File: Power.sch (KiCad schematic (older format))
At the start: 38 parts, among them J17 Power Input, Q4 YJS9435A, U6 A4403, U7 MCP16301

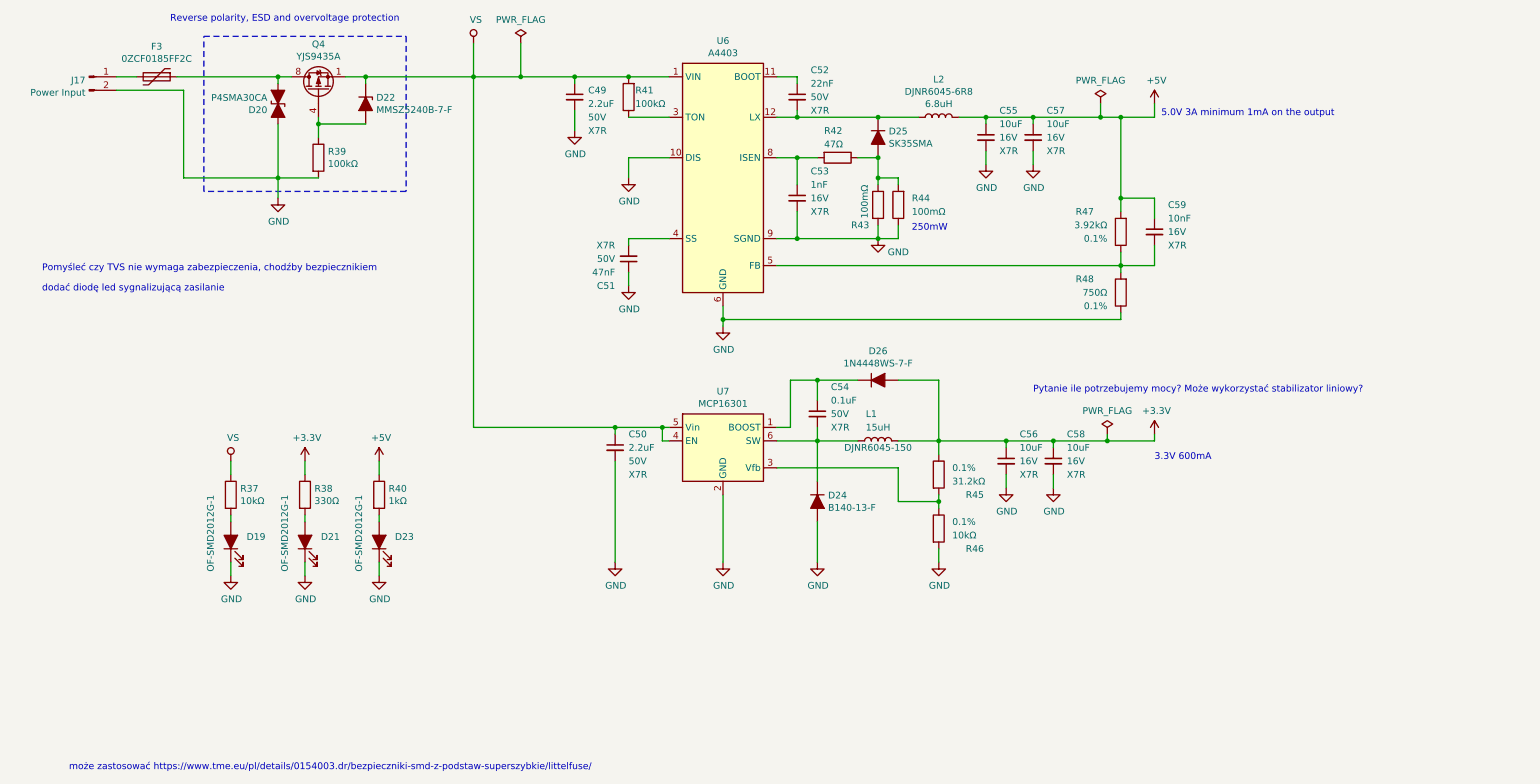
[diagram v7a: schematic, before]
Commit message: Improve Emergency, Added TVS diodes
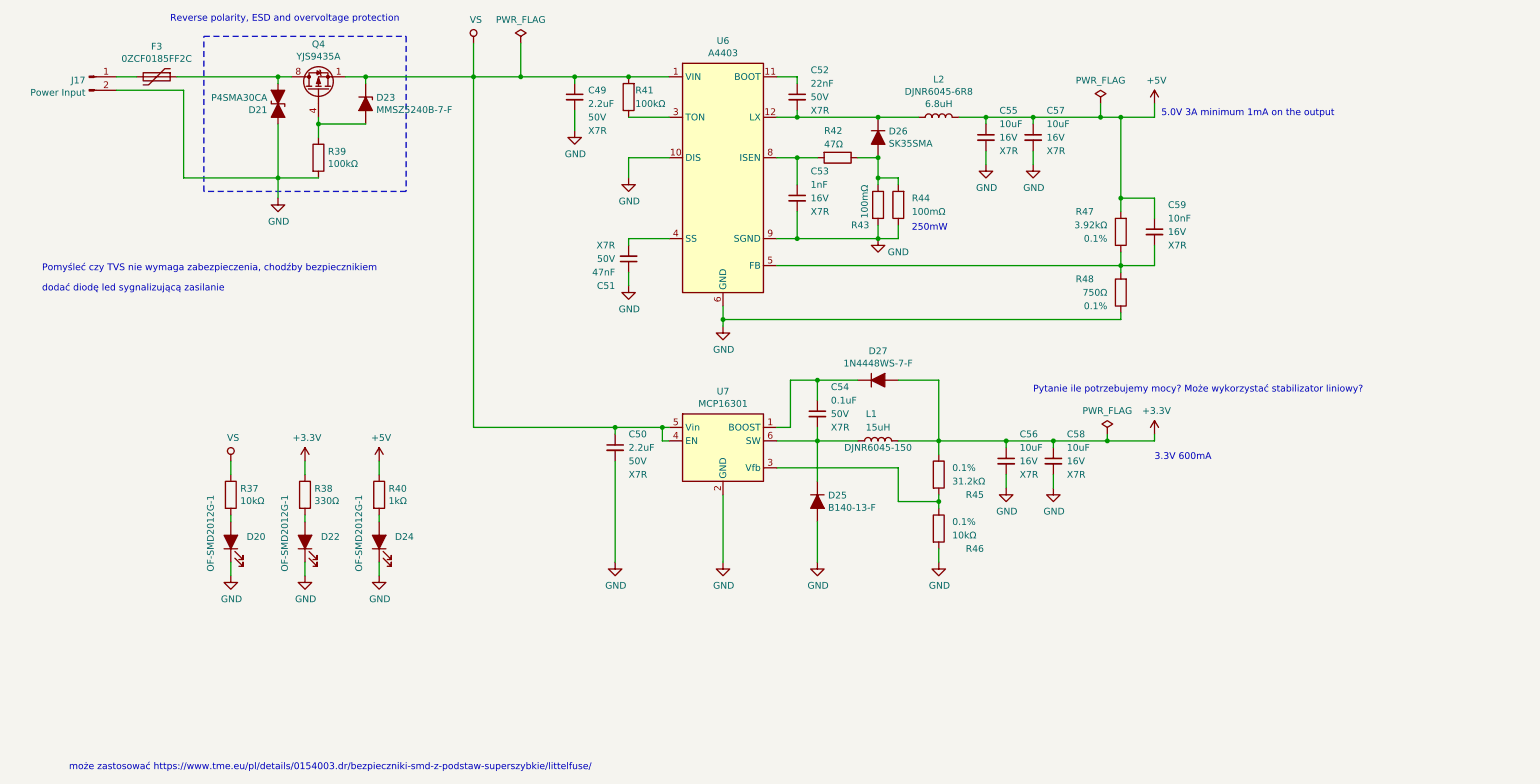
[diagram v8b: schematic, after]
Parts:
- renumbered D19 to D20, D20 to D21, D21 to D22, D22 to D23, D23 to D24, D24 to D25, D25 to D26, D26 to D27
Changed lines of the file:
@@
 Connection ~ 6250 2350
 $Comp
-L Device:D_ALT D25
+L Device:D_ALT D26
 U 1 1 5E0EF676
 P 6850 2200
-F 0 "D25" V 6804 2279 50  0000 L CNN
+F 0 "D26" V 6804 2279 50  0000 L CNN
 F 1 "SK35SMA" V 6895 2279 50  0000 L CNN
 F 2 "Diode_SMD:D_SMA" H 6850 2200 50  0001 C CNN
@@
 Connection ~ 7300 4450
 $Comp
-L Device:D_ALT D24
+L Device:D_ALT D25
 U 1 1 5E137534
 P 6400 4900
-F 0 "D24" V 6354 4979 50  0000 L CNN
+F 0 "D25" V 6354 4979 50  0000 L CNN
 F 1 "B140-13-F" V 6445 4979 50  0000 L CNN
 F 2 "Diode_SMD:D_SMA" H 6400 4900 50  0001 C CNN
@@
 $EndComp
 $Comp
-L Device:D_ALT D26
+L Device:D_ALT D27
 U 1 1 5E1551D8
 P 6850 4000
-F 0 "D26" H 6850 4216 50  0000 C CNN
+F 0 "D27" H 6850 4216 50  0000 C CNN
 F 1 "1N4448WS-7-F" H 6850 4125 50  0000 C CNN
 F 2 "Diode_SMD:D_SOD-323" H 6850 4000 50  0001 C CNN
@@
 $EndComp
 $Comp
-L Device:D_Zener_ALT D22
+L Device:D_Zener_ALT D23
 U 1 1 5E141427
 P 3050 1950
-F 0 "D22" V 3004 2029 50  0000 L CNN
+F 0 "D23" V 3004 2029 50  0000 L CNN
 F 1 "MMSZ5240B-7-F" V 3095 2029 50  0000 L CNN
 F 2 "Diode_SMD:D_SOD-123" H 3050 1950 50  0001 C CNN
@@
 	3050 1750 2900 1750
 $Comp
-L Device:D_TVS_ALT D20
+L Device:D_TVS_ALT D21
 U 1 1 5E14C395
 P 2400 1950
-F 0 "D20" V 2354 2029 50  0000 L CNN
+F 0 "D21" V 2354 2029 50  0000 L CNN
 F 1 "P4SMA30CA" V 2445 2029 50  0000 L CNN
 F 2 "Diode_SMD:D_SMA" H 2400 1950 50  0001 C CNN
@@
 $EndComp
 $Comp
-L Device:LED_ALT D23
+L Device:LED_ALT D24
 U 1 1 5E2A86AC
 P 3150 5200
-F 0 "D23" V 3189 5083 50  0000 R CNN
+F 0 "D24" V 3189 5083 50  0000 R CNN
 F 1 "OF-SMD2012G-1" H 3500 5350 50  0000 R CNN
 F 2 "Diode_SMD:D_0805_2012Metric" H 3150 5200 50  0001 C CNN
@@
 	3150 4700 3150 4600
 $Comp
-L Device:LED_ALT D19
+L Device:LED_ALT D20
 U 1 1 5E2B7376
 P 2050 5200
-F 0 "D19" V 2089 5083 50  0000 R CNN
+F 0 "D20" V 2089 5083 50  0000 R CNN
 F 1 "OF-SMD2012G-1" H 2400 5350 50  0000 R CNN
 F 2 "Diode_SMD:D_0805_2012Metric" H 2050 5200 50  0001 C CNN
@@
 	2050 4700 2050 4600
 $Comp
-L Device:LED_ALT D21
+L Device:LED_ALT D22
 U 1 1 5E28FB45
 P 2600 5200
-F 0 "D21" V 2639 5082 50  0000 R CNN
+F 0 "D22" V 2639 5082 50  0000 R CNN
 F 1 "OF-SMD2012G-1" H 2950 5350 50  0000 R CNN
 F 2 "Diode_SMD:D_0805_2012Metric" H 2600 5200 50  0001 C CNN
@@
 $EndComp
 $Comp
-L power:PWR_FLAG #FLG08
+L power:PWR_FLAG #FLG04
 U 1 1 5E49C94D
 P 8500 1950
-F 0 "#FLG08" H 8500 2025 50  0001 C CNN
+F 0 "#FLG04" H 8500 2025 50  0001 C CNN
 F 1 "PWR_FLAG" H 8500 2123 50  0000 C CNN
 F 2 "" H 8500 1950 50  0001 C CNN
@@
 $EndComp
 $Comp
-L power:PWR_FLAG #FLG09
+L power:PWR_FLAG #FLG05
 U 1 1 5E49D251
 P 8550 4400
-F 0 "#FLG09" H 8550 4475 50  0001 C CNN
+F 0 "#FLG05" H 8550 4475 50  0001 C CNN
 F 1 "PWR_FLAG" H 8550 4573 50  0000 C CNN
 F 2 "" H 8550 4400 50  0001 C CNN
@@
 	8500 2050 8650 2050
 $Comp
-L power:PWR_FLAG #FLG07
+L power:PWR_FLAG #FLG03
 U 1 1 5E4B6E09
 P 4200 1500
-F 0 "#FLG07" H 4200 1575 50  0001 C CNN
+F 0 "#FLG03" H 4200 1575 50  0001 C CNN
 F 1 "PWR_FLAG" H 4200 1673 50  0000 C CNN
 F 2 "" H 4200 1500 50  0001 C CNN
